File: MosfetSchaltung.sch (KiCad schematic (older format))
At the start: 25 parts, among them J1 Mainboard, J2 Mainboard, J3 XT60, J4 XT60, J5 XT60, Q1 IRF1404, Q2 IRF1404, Q3 IRF1404, Q4 IRF1404, Q5 IRF1404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

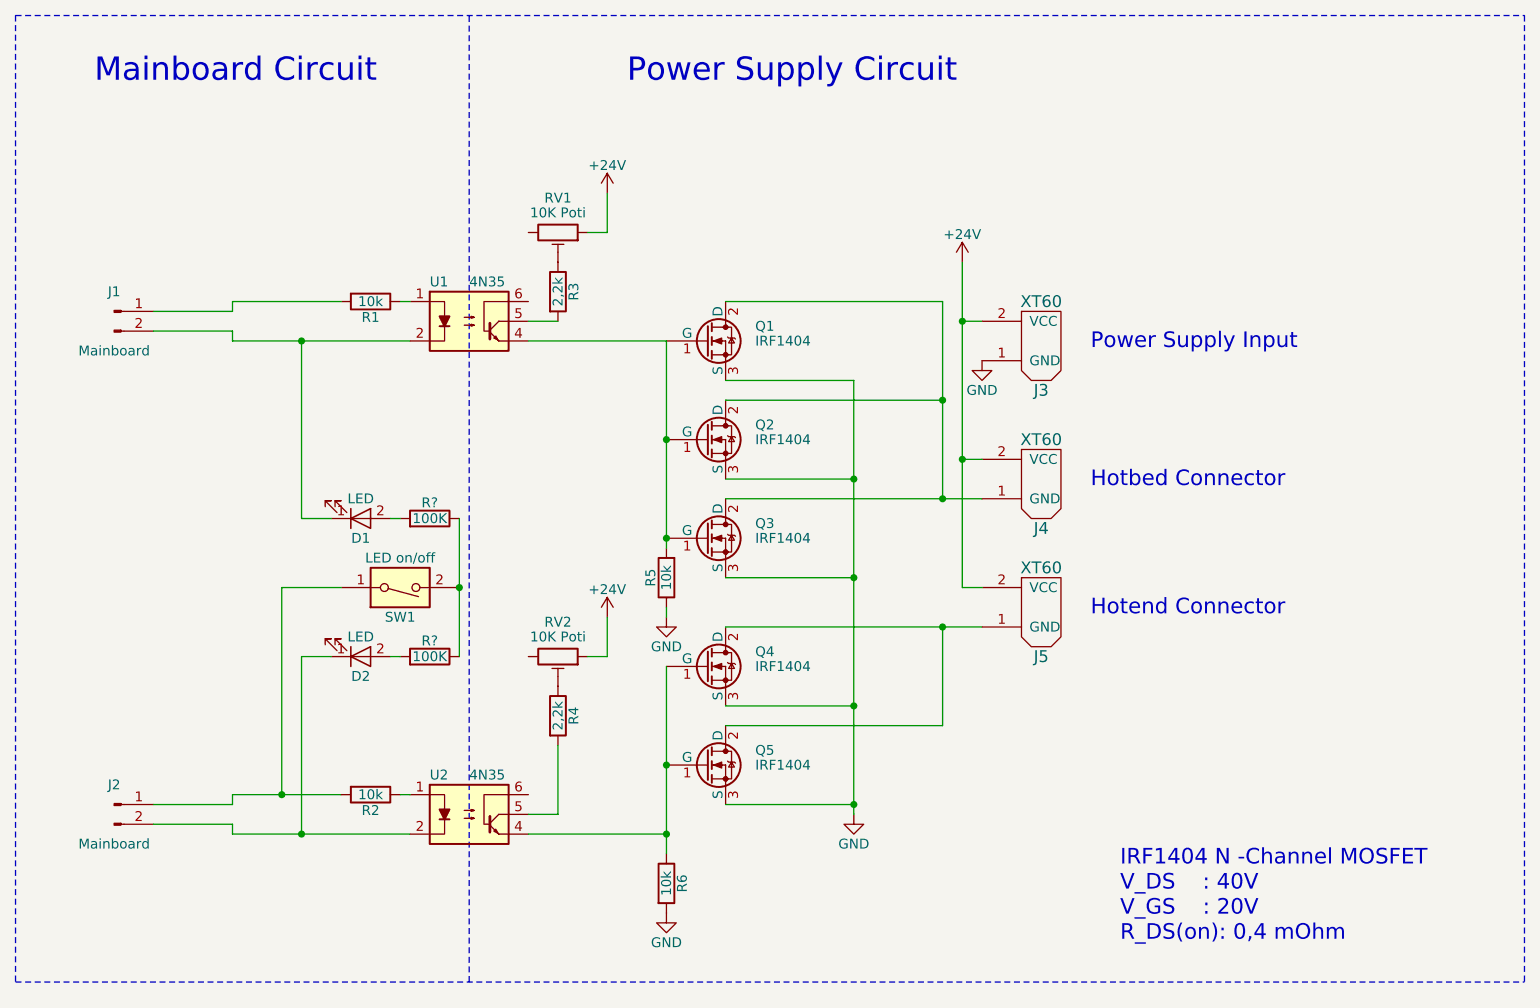
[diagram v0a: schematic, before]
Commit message: change Gate Voltage to under 15V
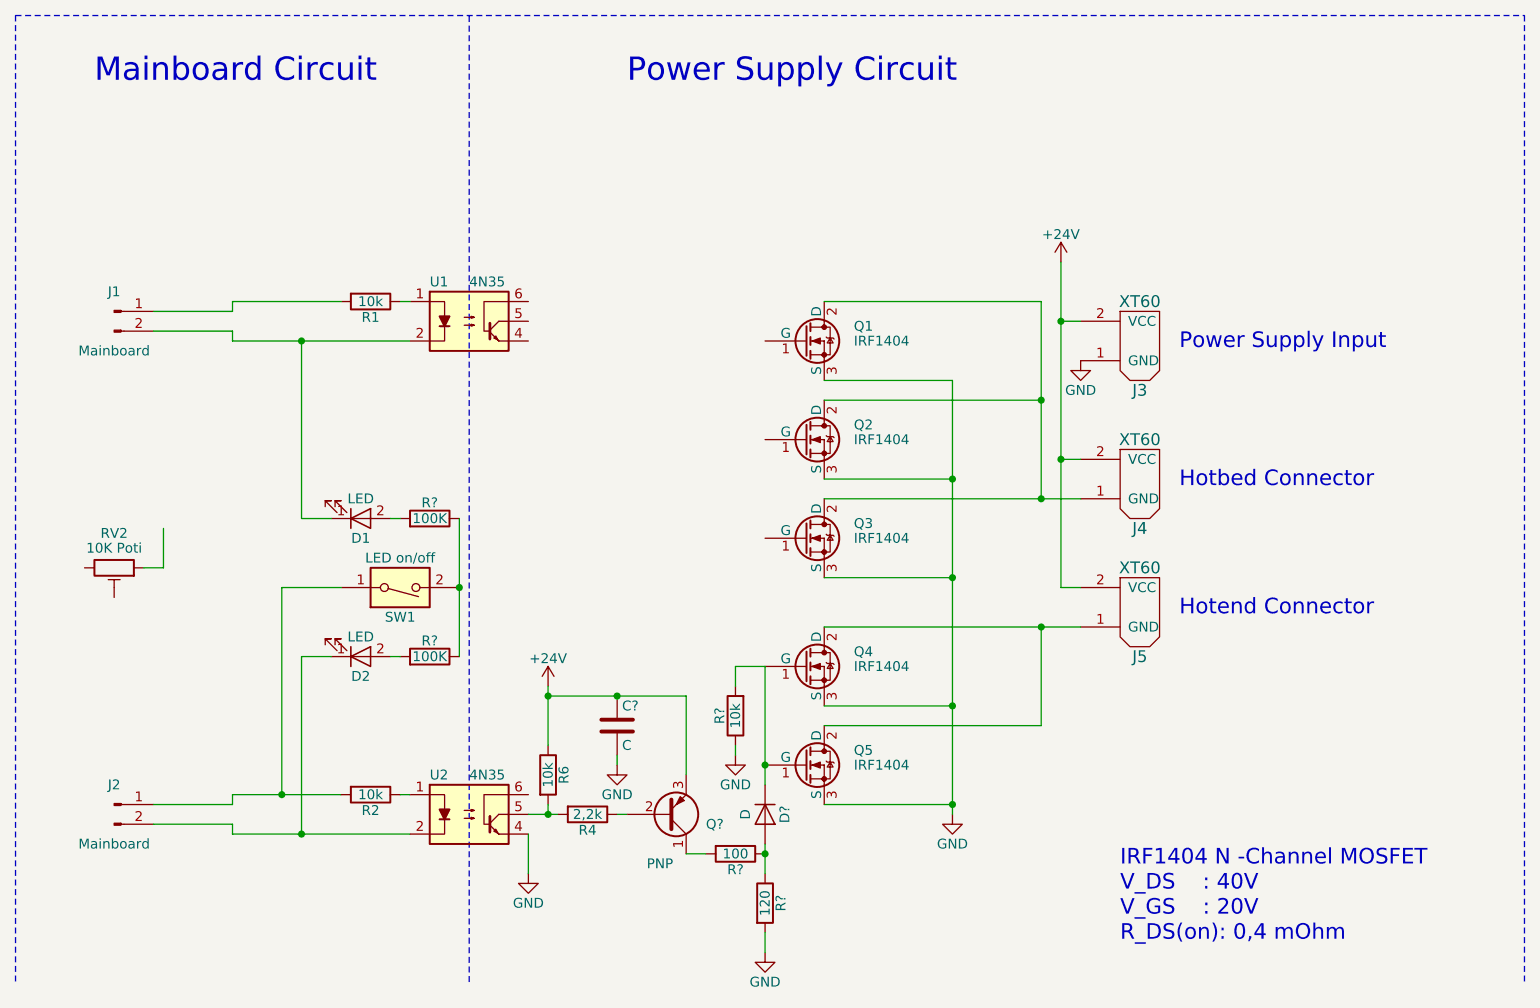
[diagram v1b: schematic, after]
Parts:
- removed R3: 2,2k, symbol R
- removed R5: 10k, symbol R
- removed RV1: 10K Poti, symbol POT_TRIM
- added C?: C, symbol C
- added D?: D, symbol D
- added Q?: PNP, symbol Q_PNP_CBE
- added R?: 10k, symbol R
- added R?: 100, symbol R
- added R?: 120, symbol R
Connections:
- net +24V: now also R6.1, C?.1, Q?.3 (E); no longer RV2.1
- net GND: now also U2.4, C?.2, R?.1, R?.2; no longer R6.2
- net at Q4.1 (G), Q5.1 (G): now also D?.1 (K), R?.2; no longer R6.1, U2.4
- net at R4.2, U2.5: now also R6.2
- net at R4.1: now also Q?.2 (B); no longer RV2.2
- new net: Q?.1 (C), R?.2
- new net: D?.2 (A), R?.1, R?.1
- now unconnected: Q1.1 (G), Q2.1 (G), Q3.1 (G), U1.4
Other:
- moved on the sheet: J3, J4, J5, Q1, Q2, Q3, Q4, Q5, R4, R6, RV2
